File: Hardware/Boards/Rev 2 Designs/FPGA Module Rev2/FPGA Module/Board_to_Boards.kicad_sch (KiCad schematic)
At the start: 2 parts, among them J1 LSHM-130-XX.X-XXX-DV-A-S-K-XX, J2 LSHM-130-XX.X-XXX-DV-A-S-K-XX

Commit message: FPGA Module Rev 2 Layout Begun
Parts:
- renumbered J2 to J1, J1 to J2
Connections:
- net HDMI_D2_P is gone; now on net GND: J1.33
- net MBUS_D12 is gone; now on net MBUS_D8: J2.21
- net MBUS_D13 is gone; now on net MBUS_D7: J2.23
- net MBUS_D14 is gone; now on net MBUS_D6: J2.25
- net CAM_LED_EN: now also J2.03; no longer J1.04
- net CAM_PWR_EN: now also J2.01; no longer J1.02
- net FIFO_BE0: now also J2.43; no longer J2.34
- net FIFO_BE1: now also J2.41; no longer J2.32
- net FIFO_CLK: now also J2.30; no longer J2.36
- net FIFO_D0: now also J2.14; no longer J2.52
- net FIFO_D1: now also J2.16; no longer J2.50
- net FIFO_D10: now also J2.36; no longer J2.41
- net FIFO_D11: now also J2.38; no longer J2.39
- net FIFO_D12: now also J2.51; no longer J2.37
- net FIFO_D13: now also J2.49; no longer J2.35
- net FIFO_D14: now also J2.47; no longer J2.33
- net FIFO_D15: now also J2.45; no longer J2.31
- net FIFO_D2: now also J2.18; no longer J2.48
- net FIFO_D3: now also J2.20; no longer J2.46
- net FIFO_D4: now also J2.22; no longer J2.44
- net FIFO_D5: now also J2.24; no longer J2.42
- net FIFO_D6: now also J2.26; no longer J2.40
- net FIFO_D7: now also J2.28; no longer J2.38
- net FIFO_D8: now also J2.32; no longer J2.45
- net FIFO_D9: now also J2.34; no longer J2.43
- net FPGA_I2C_SCL: now also J1.20; no longer J2.01
- net FPGA_I2C_SDA: now also J1.18; no longer J2.03
- net FT600_OE: now also J2.48; no longer J1.28
- net FT600_RD: now also J2.46; no longer J2.49
- net FT600_RST: now also J2.50; no longer J1.26
- net FT600_RXE: now also J2.42; no longer J1.30
- net FT600_TXE: now also J2.40; no longer J1.32
- net FT600_WAKEUP: now also J2.52; no longer J1.24
- net FT600_WR: now also J2.44; no longer J2.51
- net GND: now also J2.13, J2.39; no longer J1.06, J1.08, J1.10, J1.12, J1.14, J1.16, J1.18, J1.20, J1.34, J1.37, J1.43, J1.49, J1.55, J1.57, J2.27, J2.29, J2.30, J2.47
- net MBUS_D0: now also J2.37; no longer J2.14
- net MBUS_D1: now also J2.35; no longer J2.16
- net MBUS_D11: now also J2.15; no longer J2.19
- net MBUS_D2: now also J2.33; no longer J2.18
- net MBUS_D3: now also J2.31; no longer J2.20
- net MBUS_D4: now also J2.29; no longer J2.22
- net MBUS_D5: now also J2.27; no longer J2.24
- net MBUS_D6: no longer J2.26
- net MBUS_D7: no longer J2.28
- net MBUS_D8: no longer J2.13
- net MBUS_D9: now also J2.19; no longer J2.15
- net USB_SYSMON_D_N: now also J2.07; no longer J2.09
- net USB_SYSMON_D_P: now also J2.09; no longer J2.07
- net HDMI_CEC renamed HDMI_DB7
- net HDMI_CLK_N renamed HDMI_DR5
- net HDMI_CLK_P renamed HDMI_DR4
- net HDMI_D0_N renamed HDMI_DR2
- net HDMI_D0_P renamed HDMI_DR1
- net HDMI_D1_N renamed HDMI_DE
- net HDMI_D1_P renamed HDMI_HSYNC
- net HDMI_D2_N renamed HDMI_IDCLK
- net HDMI_EQ_SEL renamed HDMI_DG6
- net HDMI_HPD_SRC renamed HDMI_DG4
- net HDMI_I2C_EN renamed HDMI_DG7
- net HDMI_OE renamed HDMI_DG2
- net HDMI_PRE_SEL renamed HDMI_DG5
- net HDMI_SCL_SRC renamed HDMI_DB5
- net HDMI_SDA_SRC renamed HDMI_DB4
- net HDMI_SDA_SRC_EN renamed HDMI_DB6
- net HDMI_SEL renamed HDMI_DG3
- net HDMI_SLEW_CTL renamed HDMI_DG1
- net TPD5_EN renamed HDMI_DG0
- new net HDMI_DB0: J1.28
- new net HDMI_DB1: J1.30
- new net HDMI_DB2: J1.32
- new net HDMI_DB3: J1.34
- new net HDMI_DR0: J1.43
- new net HDMI_DR3: J1.49
- new net HDMI_DR6: J1.55
- new net HDMI_DR7: J1.57
- new net HDMI_INT: J1.24
- new net HDMI_MCLK: J1.16
- new net HDMI_RST: J1.26
- new net HDMI_SCK: J1.14
- new net HDMI_SD0_DL0: J1.10
- new net HDMI_SD1_DR1: J1.08
- new net HDMI_SD2_DL1: J1.06
- new net HDMI_SD3_DR2: J1.04
- new net HDMI_SPDIF: J1.02
- new net HDMI_VSYNC: J1.37
- new net HDMI_WS_DR0: J1.12
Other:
- note removed: "FPGA GTY XCVR (1V2)"
- note removed: "FPGA GTY XCVR (1V2) OR FPGA 1V8 LVDS"
- moved on the sheet: J1, J2

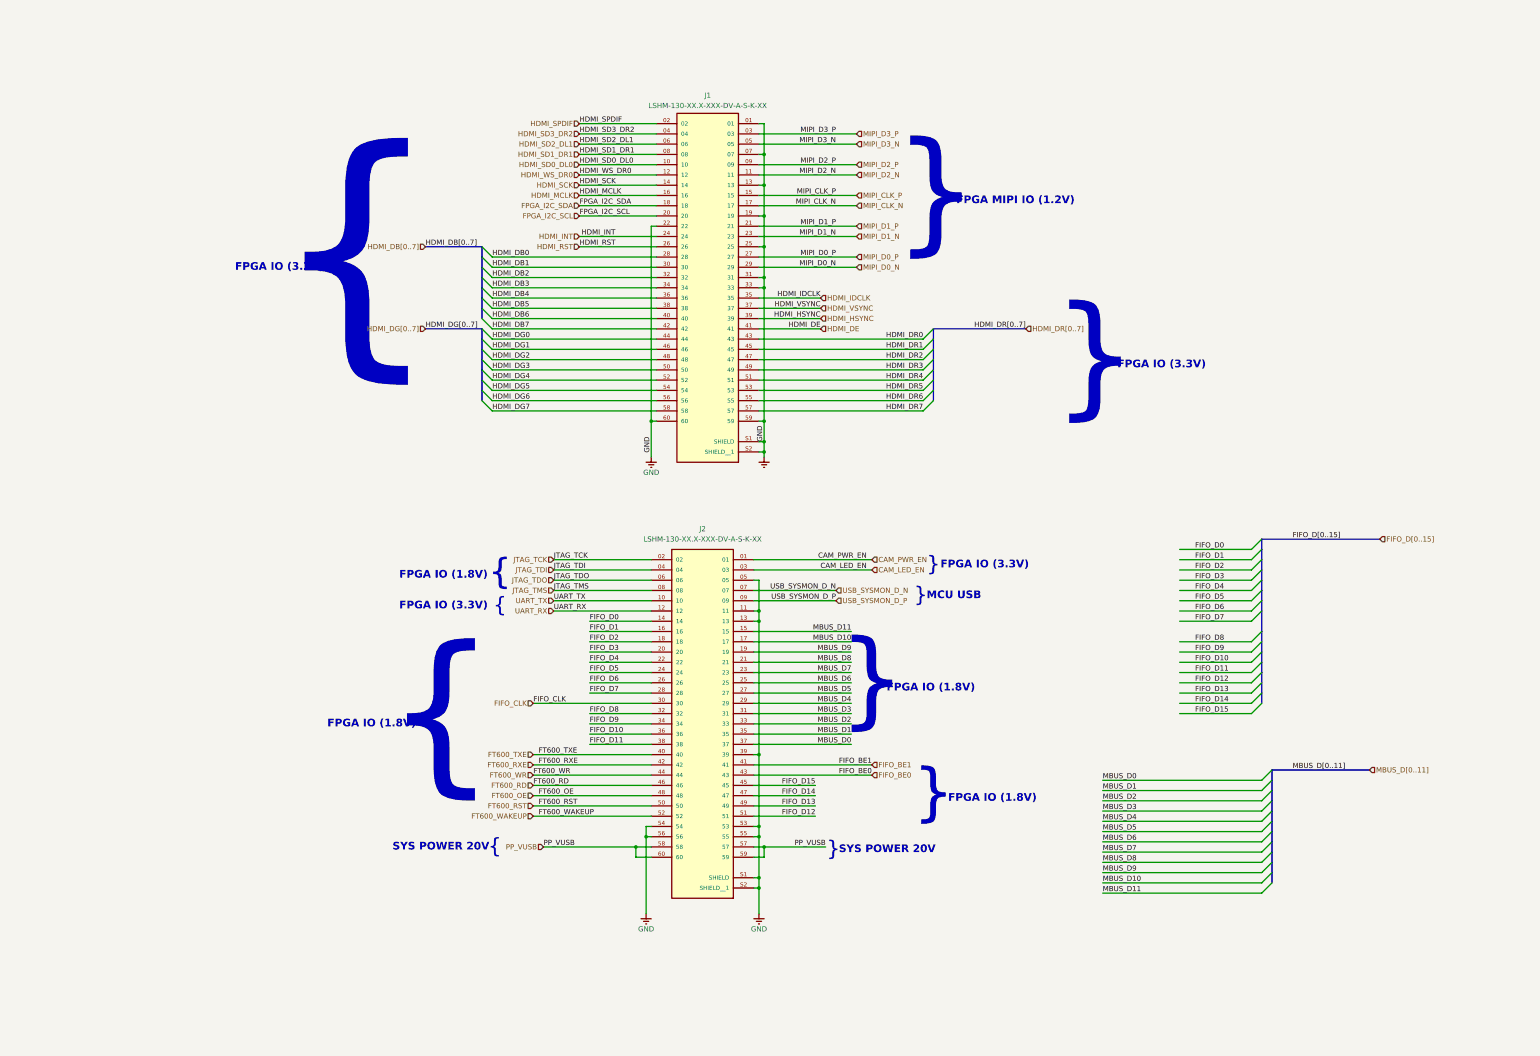
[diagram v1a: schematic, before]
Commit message: Completed B2B and HyperRam routing
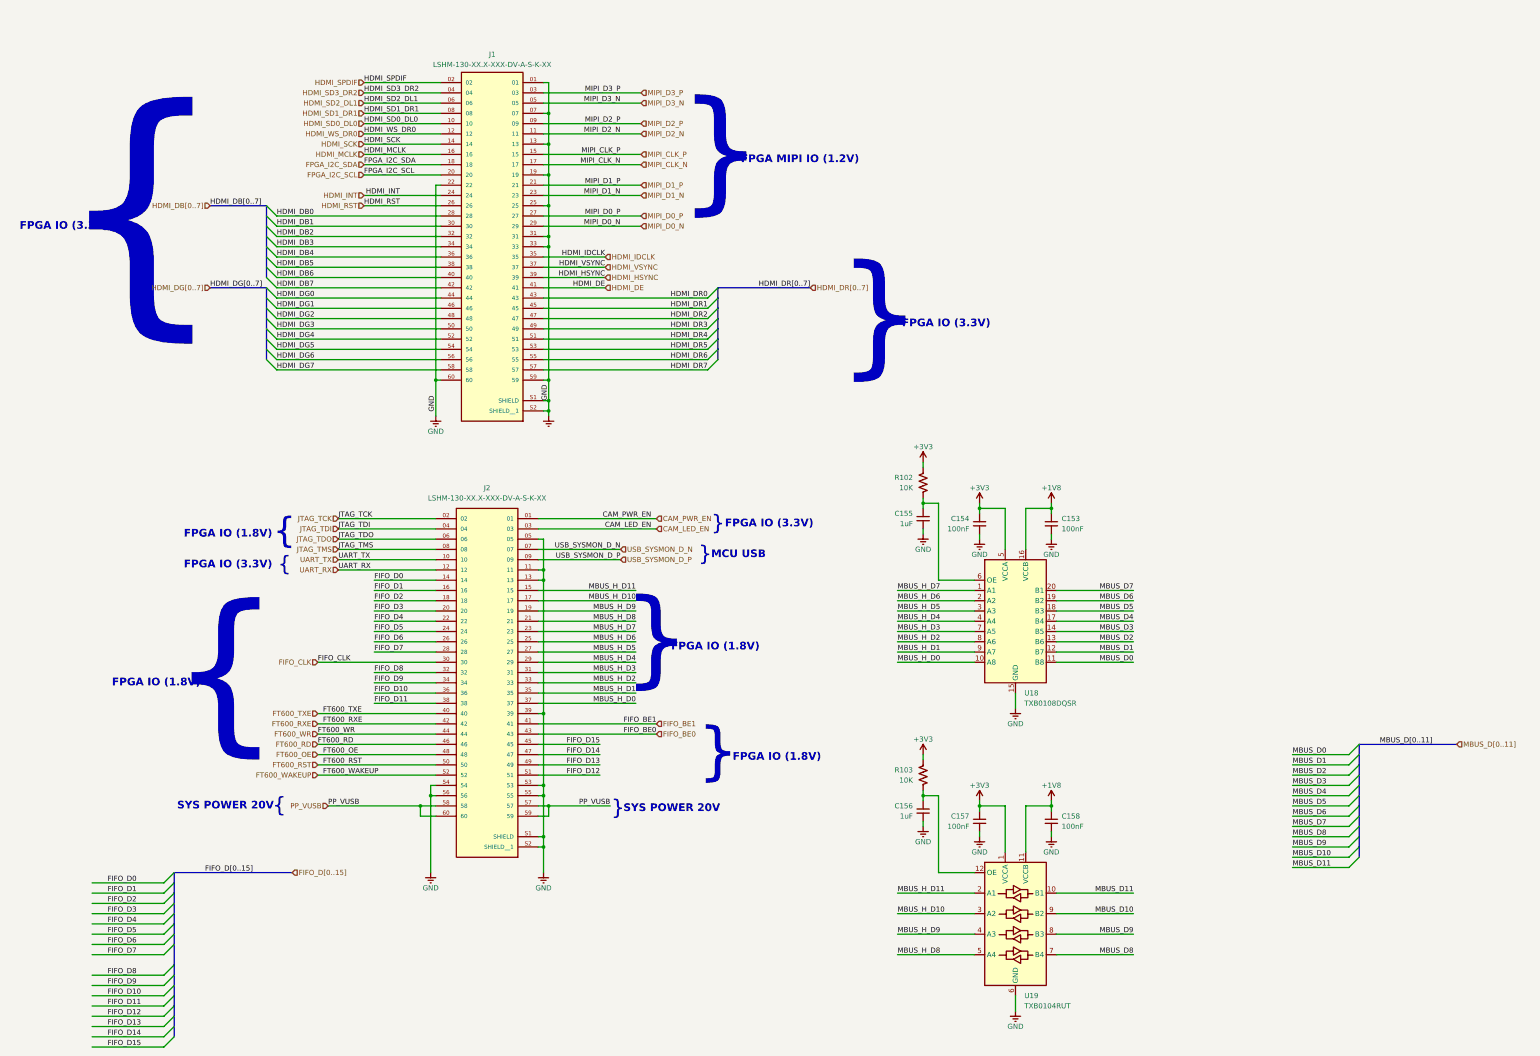
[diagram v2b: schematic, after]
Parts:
- added C153, C154, C157, C158: 100nF, Capacitor_SMD:C_0201_0603Metric, symbol Device:C_Small
- added C155, C156: 1uF, Capacitor_SMD:C_0201_0603Metric, symbol Device:C_Small
- added R102, R103: 10K, Resistor_SMD:R_0201_0603Metric, symbol Device:R_US
- added U18: TXB0108DQSR, Package_SON:USON-20_2x4mm_P0.4mm, symbol Logic_LevelTranslator:TXB0108DQSR
- added U19: TXB0104RUT, Package_DFN_QFN:Texas_R-PUQFN-N12, symbol Logic_LevelTranslator:TXB0104RUT
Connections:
- net GND: now also C153.2, C154.2, C155.2, C156.2, C157.2, C158.2, U18.15 (GND), U19.6 (GND)
- net MBUS_D0: now also U18.11 (B8); no longer J2.37
- net MBUS_D1: now also U18.12 (B7); no longer J2.35
- net MBUS_D10: now also U19.9 (B2); no longer J2.17
- net MBUS_D11: now also U19.10 (B1); no longer J2.15
- net MBUS_D2: now also U18.13 (B6); no longer J2.33
- net MBUS_D3: now also U18.14 (B5); no longer J2.31
- net MBUS_D4: now also U18.17 (B4); no longer J2.29
- net MBUS_D5: now also U18.18 (B3); no longer J2.27
- net MBUS_D6: now also U18.19 (B2); no longer J2.25
- net MBUS_D7: now also U18.20 (B1); no longer J2.23
- net MBUS_D8: now also U19.7 (B4); no longer J2.21
- net MBUS_D9: now also U19.8 (B3); no longer J2.19
- new net: C155.1, R102.1, U18.6 (OE)
- new net: C156.1, R103.1, U19.12 (OE)
- new net +1V8: C153.1, C158.1, U18.16 (VCCB), U19.11 (VCCB)
- new net +3V3: C154.1, C157.1, R102.2, R103.2, U18.5 (VCCA), U19.1 (VCCA)
- new net MBUS_H_D0: J2.37, U18.10 (A8)
- new net MBUS_H_D1: J2.35, U18.9 (A7)
- new net MBUS_H_D10: J2.17, U19.3 (A2)
- new net MBUS_H_D11: J2.15, U19.2 (A1)
- new net MBUS_H_D2: J2.33, U18.8 (A6)
- new net MBUS_H_D3: J2.31, U18.7 (A5)
- new net MBUS_H_D4: J2.29, U18.4 (A4)
- new net MBUS_H_D5: J2.27, U18.3 (A3)
- new net MBUS_H_D6: J2.25, U18.2 (A2)
- new net MBUS_H_D7: J2.23, U18.1 (A1)
- new net MBUS_H_D8: J2.21, U19.5 (A4)
- new net MBUS_H_D9: J2.19, U19.4 (A3)
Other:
- moved on the sheet: J1, J2
